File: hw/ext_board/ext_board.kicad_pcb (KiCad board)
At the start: 2 copper layers, 61 x 53.3 mm, 55 parts, among them Q1 SS8050, Q2 SS8050, Q3 SS8050, Q4 SS8050, Q5 SS8050, Q6 SS8050, Q7 SS8050, Q8 SS8050, Q9 SS8050, U1 74HC595PW, U2 74HC595PW, U3 M24LC16, U4 M93C76, X1 UNO_R3_CONN

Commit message: Add layout
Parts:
- added J1: Conn_01x03, Pin_Headers:Pin_Header_Straight_1x03_Pitch2.54mm, F.Cu at (127.0, 97.8)
- added J2: Conn_01x05, Pin_Headers:Pin_Header_Straight_1x05_Pitch2.54mm, F.Cu at (132.6, 97.8)
- added J3: Conn_01x03, Pin_Headers:Pin_Header_Straight_1x03_Pitch2.54mm, F.Cu at (180.3, 63.5)
- added J4: Conn_01x02, Pin_Headers:Pin_Header_Straight_1x02_Pitch2.54mm, F.Cu at (127.0, 111.2)
- added LD2: RGBW, ext_board:GNL-5050WRGB, F.Cu at (171.3, 91.4)
- C1, C2, C3, C4, C5, C6, D1, Q5, Q6, Q7, Q8, Q9, R1, R10, R11, R12, R13, R14, R15, R16, R17, R18, R19, R2, R20, R21, R22, R23, R24, R25, R26, R27, R7, R8, R9, U1, U2, U3, U4: moved to B.Cu
- moved C3 98.0 mm to (127.3, 70.1), turned to 180 degrees
- moved C1 92.0 mm to (155.8, 67.8), turned to 180 degrees
- moved R16 89.5 mm to (127.8, 68.1), turned to 180 degrees
- moved C2 89.4 mm to (164.0, 67.8), turned to 180 degrees
- moved C4 82.5 mm to (130.9, 80.6)
- moved R15 82.5 mm to (127.8, 66.3), turned to 180 degrees
- moved C6 78.8 mm to (169.0, 79.4), turned to 270 degrees
- moved R9 73.0 mm to (144.8, 85.7), turned to 270 degrees
- moved R19 69.0 mm to (178.6, 88.9), turned to 90 degrees
- moved R8 68.1 mm to (149.9, 77.1), turned to 270 degrees
- moved R12 67.0 mm to (141.9, 77.1), turned to 270 degrees
- moved R10 65.5 mm to (139.7, 85.7), turned to 270 degrees
- moved Q8 65.0 mm to (175.2, 95.5), turned to 180 degrees
- moved R13 62.0 mm to (147.3, 85.7), turned to 270 degrees
- moved R26 56.6 mm to (174.2, 82.8), turned to 90 degrees
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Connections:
- B1 pad 4: Net-(B1-Pad4) -> /QH2
- B2 pad 4: Net-(B2-Pad4) -> /QG2
- B3 pad 4: Net-(B3-Pad4) -> /QF2
- B4 pad 4: Net-(B4-Pad4) -> /QE2
- Q5 pad 3: (no net) -> Net-(LD2-Pad1)
- Q6 pad 3: (no net) -> Net-(LD2-Pad2)
- Q8 pad 3: (no net) -> Net-(LD2-Pad3)
- Q9 pad 3: (no net) -> Net-(LD2-Pad4)
- R10 pad 2: Net-(R10-Pad2) -> /QE1
- R11 pad 2: Net-(R11-Pad2) -> /QD1
- R12 pad 2: Net-(R12-Pad2) -> /QC1
- R13 pad 2: Net-(R13-Pad2) -> /QB1
- R14 pad 2: Net-(R14-Pad2) -> /QA1
- R23 pad 1: (no net) -> Net-(LD2-Pad8)
- R24 pad 1: (no net) -> Net-(LD2-Pad7)
- R26 pad 1: (no net) -> Net-(LD2-Pad6)
- R27 pad 1: (no net) -> Net-(LD2-Pad5)
- R3 pad 2: Net-(R3-Pad2) -> /QA2
- R4 pad 2: Net-(R4-Pad2) -> /QB2
- R5 pad 2: Net-(R5-Pad2) -> /QC2
- R6 pad 2: Net-(R6-Pad2) -> /QD2
- R7 pad 2: Net-(R7-Pad2) -> /QH1
- R8 pad 2: Net-(R8-Pad2) -> /QG1
- R9 pad 2: Net-(R9-Pad2) -> /QF1
- U1 pad 1: Net-(R13-Pad2) -> /QD2
- U1 pad 15: Net-(R14-Pad2) -> /QH2
- U1 pad 2: Net-(R12-Pad2) -> /QA2
- U1 pad 3: Net-(R11-Pad2) -> /QH1
- U1 pad 4: Net-(R10-Pad2) -> /QC1
- U1 pad 5: Net-(R9-Pad2) -> /QB2
- U1 pad 6: Net-(R8-Pad2) -> /QC2
- U1 pad 7: Net-(R7-Pad2) -> /QG1
- U2 pad 1: Net-(R4-Pad2) -> /QF2
- U2 pad 15: Net-(R3-Pad2) -> /QG2
- U2 pad 2: Net-(R5-Pad2) -> /QE2
- U2 pad 3: Net-(R6-Pad2) -> /QD1
- U2 pad 4: Net-(B4-Pad4) -> /QE1
- U2 pad 5: Net-(B3-Pad4) -> /QA1
- U2 pad 6: Net-(B2-Pad4) -> /QF1
- U2 pad 7: Net-(B1-Pad4) -> /QB1
- X1 pad 15: (no net) -> /RX
- X1 pad 16: (no net) -> /TX
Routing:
- net GND: track 0.00 -> 207.3 mm, vias 0 -> 14
- net +5V: track 0.00 -> 196.4 mm, vias 0 -> 8
- net /KEY: track 0.00 -> 96.6 mm, vias 0 -> 2
- net /SCK: track 0.00 -> 82.0 mm, vias 0 -> 1
- net /MOSI: track 0.00 -> 69.4 mm, vias 0 -> 2
- net /QH2: track 0.00 -> 55.9 mm, vias 0 -> 3
- net /~CS: track 0.00 -> 47.9 mm, vias 0 -> 1
- net /SDA: track 0.00 -> 45.9 mm, vias 0 -> 1
- net /MISO: track 0.00 -> 43.8 mm, vias 0 -> 1
- net /QD1: track 0.00 -> 38.8 mm
- net /CLK: track 0.00 -> 38.0 mm, vias 0 -> 1
- net Net-(R22-Pad1): track 0.00 -> 38.0 mm
- net /LEDW: track 0.00 -> 38.0 mm, vias 0 -> 1
- net /QE2: track 0.00 -> 37.4 mm, vias 0 -> 1
- net /QG2: track 0.00 -> 35.6 mm, vias 0 -> 1
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- added copper zone on B.Cu, net GND
- added copper zone on F.Cu, net GND
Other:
- net class Default: trace_width 0.25 -> 0.35; via_dia 0.6 -> 1; via_drill 0.4 -> 0.5
- rule via_min_size: 0.4 -> 0.9

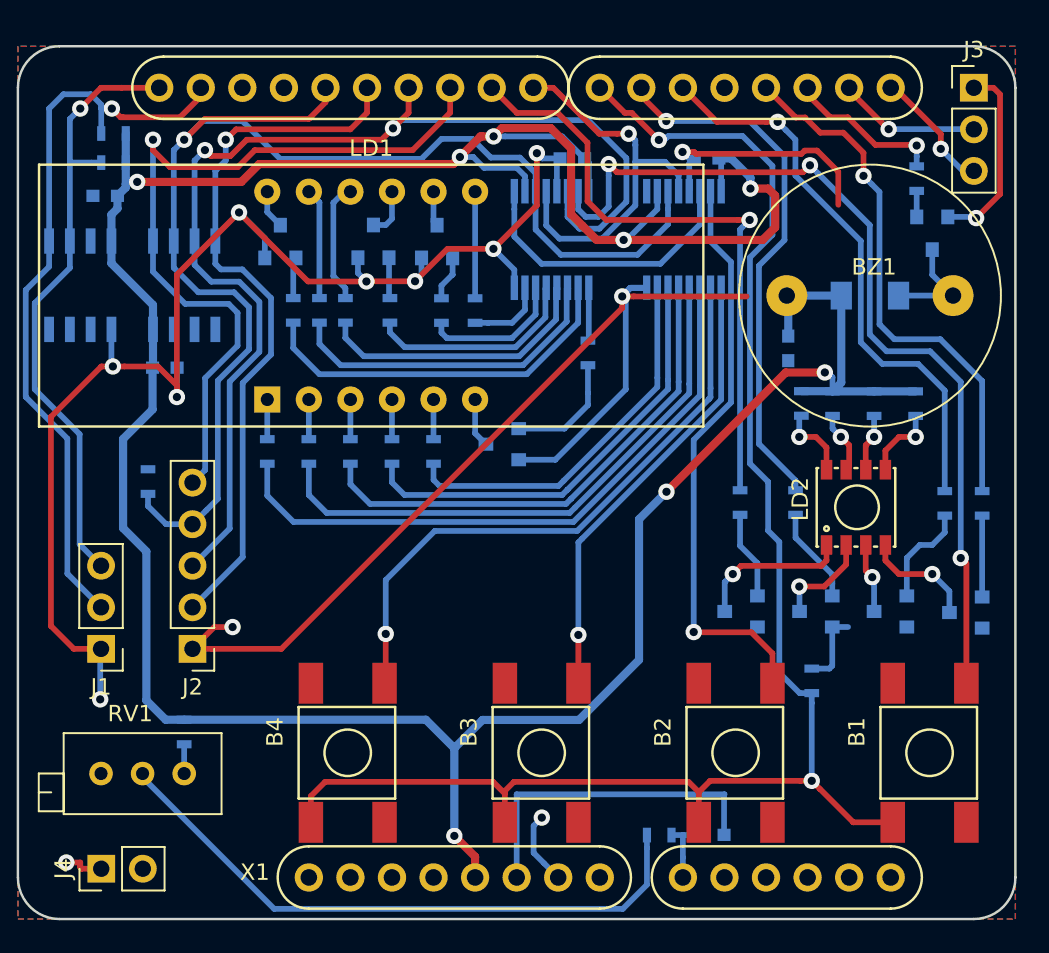
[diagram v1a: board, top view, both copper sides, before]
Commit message: Change buttons to TH
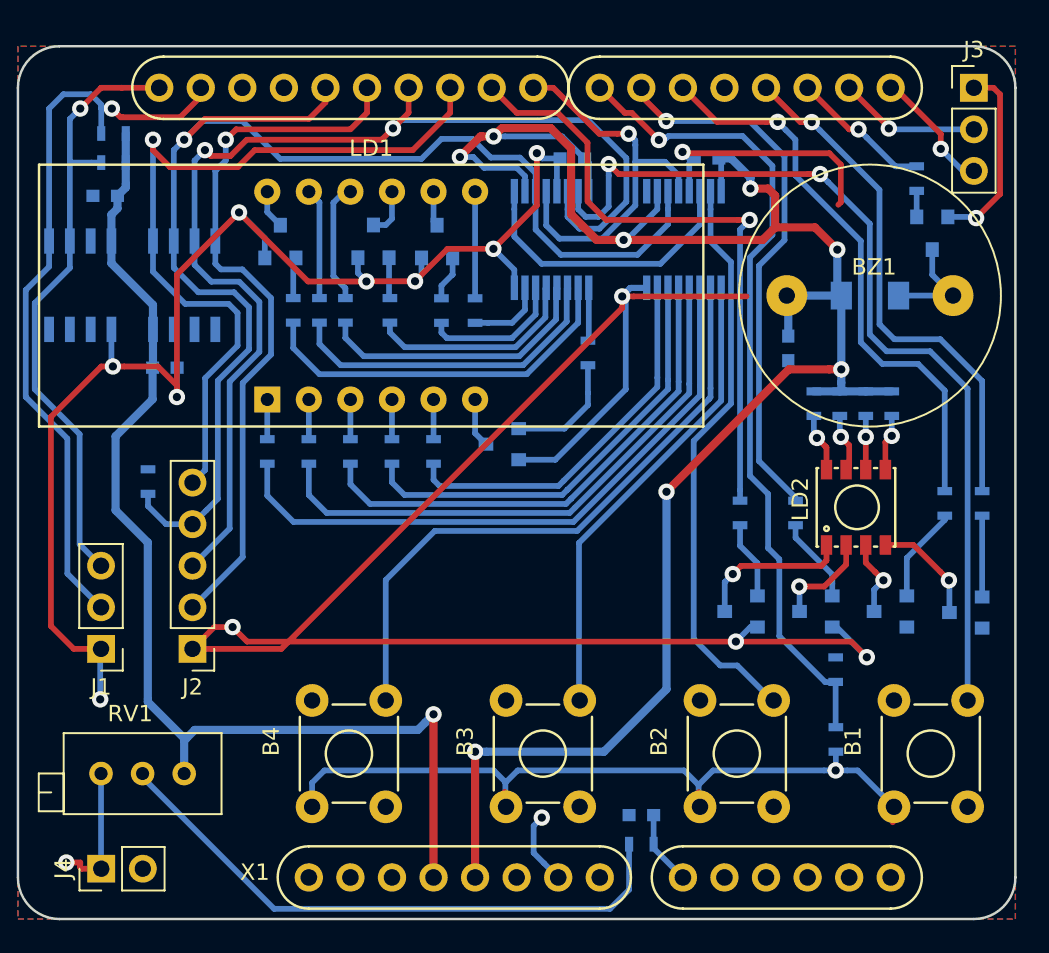
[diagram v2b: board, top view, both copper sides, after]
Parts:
- B1, B2, B3, B4: footprint ext_board:IT-1102WB_6x6x7 -> ext_board:KLS7-TS6601_6x6x4.3
- R25: value 6.7k -> 6.8k
- moved R25 39.8 mm to (171.9, 103.3), turned to 270 degrees
- moved C5 4.47 mm to (160.0, 108.0), turned to 180 degrees
- moved B3 3.95 mm to (151.8, 107.4)
- moved B4 3.95 mm to (139.9, 107.4)
- moved B1 3.95 mm to (175.5, 107.4)
- moved B2 3.95 mm to (163.6, 107.4)
- moved R2 1.61 mm to (171.9, 99.1)
- moved R27 1.46 mm to (175.3, 82.8)
- moved R22 1.23 mm to (160.0, 109.7)
- moved R23 0.76 mm to (170.6, 82.8)
- moved R17 0.64 mm to (166.1, 89.5)
- moved R18 0.64 mm to (169.4, 89.5)
- moved R26 0.51 mm to (173.7, 82.8)
- moved R24 0.44 mm to (172.1, 82.8)
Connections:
- net /QA1 renamed /LED_DP
- net /QA2 renamed /LED_1
- net /QB1 renamed /LED_G
- net /QB2 renamed /LED_2
- net /QC1 renamed /LED_F
- net /QC2 renamed /LED_3
- net /QD1 renamed /LED_E
- net /QD2 renamed /LED_4
- net /QE1 renamed /LED_D
- net /QE2 renamed /KEY_B4
- net /QF1 renamed /LED_C
- net /QF2 renamed /KEY_B3
- net /QG1 renamed /LED_B
- net /QG2 renamed /KEY_B2
- net /QH1 renamed /LED_A
- net /QH2 renamed /KEY_B1
- B1 pad 1: /KEY -> Net-(B1-Pad1)
- B2 pad 1: /KEY -> Net-(B1-Pad1)
- B3 pad 1: /KEY -> Net-(B1-Pad1)
- B4 pad 1: /KEY -> Net-(B1-Pad1)
- C3 pad 1: +5V -> +3V3
- C4 pad 1: +5V -> +3V3
- R15 pad 1: +5V -> +3V3
- R16 pad 1: +5V -> +3V3
- R25 pad 1: Net-(R25-Pad1) -> /KEY
- R25 pad 2: +5V -> Net-(B1-Pad1)
- RV1 pad 1: Net-(R25-Pad1) -> +3V3
- U3 pad 8: +5V -> +3V3
- U4 pad 8: +5V -> +3V3
- X1 pad 4: (no net) -> +3V3
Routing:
- net +5V: track 196.4 -> 122.4 mm
- net +3V3: track 0.00 -> 69.1 mm, vias 0 -> 1
- net /KEY: track 96.6 -> 50.5 mm, vias 2 -> 1
- net Net-(B1-Pad1): track 0.00 -> 45.4 mm, vias 0 -> 1
- net GND: track 207.3 -> 232.6 mm, vias 14 -> 16
- net Net-(R25-Pad1): track 1.79 -> 0.00 mm
- net Net-(R22-Pad1): track 38.0 -> 36.6 mm
- net Net-(LD2-Pad5): track 4.65 -> 3.45 mm
- net /KEY_B4: track 37.4 -> 38.5 mm, vias 1 -> 0
- net /KEY_B3: track 27.8 -> 28.8 mm, vias 1 -> 0
- net Net-(LD2-Pad8): track 4.64 -> 3.61 mm
- net /PWM: track 9.64 -> 8.66 mm
- net /KEY_B1: track 55.9 -> 56.7 mm, vias 3 -> 2
- net /LEDR: track 32.9 -> 32.2 mm
- net /LEDB: track 33.3 -> 33.9 mm
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
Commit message: Add reference signes
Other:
- board size 61 x 53.3 mm -> 63.5 x 55.9 mm
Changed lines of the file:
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@@
     (links 139)
     (no_connects 0)
-    (area 121.844999 60.884999 182.955001 114.375001)
+    (area 110.484367 54.45 189.095953 115.974219)
     (thickness 1.6)
-    (drawings 10)
+    (drawings 22)
     (tracks 683)
     (zones 0)
@@
     (34 B.Paste user)
     (35 F.Paste user)
-    (36 B.SilkS user hide)
+    (36 B.SilkS user)
     (37 F.SilkS user)
     (38 B.Mask user)
@@
     (46 B.CrtYd user)
     (47 F.CrtYd user)
-    (48 B.Fab user hide)
-    (49 F.Fab user hide)
+    (48 B.Fab user)
+    (49 F.Fab user)
   )
   (setup
@@
     (trace_min 0.2)
     (segment_width 0.2)
-    (edge_width 0.15)
+    (edge_width 0.1)
     (via_size 1)
     (via_drill 0.5)
@@
     (pad_to_mask_clearance 0.2)
     (aux_axis_origin 121.92 114.3)
-    (visible_elements FFFFFF7F)
+    (visible_elements FFFFFFFF)
     (pcbplotparams
       (layerselection 0x00030_80000001)
@@
     (pad 3 thru_hole circle (at 0 4.5 90) (size 2 2) (drill 1) (layers *.Cu *.Mask))
   )
+  (gr_line (start 120.65 60.96) (end 123.19 60.96) (layer Edge.Cuts) (width 0.1))
+  (gr_line (start 121.92 59.69) (end 121.92 62.23) (layer Edge.Cuts) (width 0.1))
+  (gr_circle (center 121.92 60.96) (end 122.555 60.96) (layer Edge.Cuts) (width 0.1))
+  (gr_line (start 181.61 60.96) (end 184.15 60.96) (layer Edge.Cuts) (width 0.1))
+  (gr_line (start 182.88 59.69) (end 182.88 62.23) (layer Edge.Cuts) (width 0.1))
+  (gr_circle (center 182.88 60.96) (end 183.515 60.96) (layer Edge.Cuts) (width 0.1))
+  (gr_line (start 181.61 114.3) (end 184.15 114.3) (layer Edge.Cuts) (width 0.1))
+  (gr_line (start 182.88 113.03) (end 182.88 115.57) (layer Edge.Cuts) (width 0.1))
+  (gr_circle (center 182.88 114.3) (end 183.515 114.3) (layer Edge.Cuts) (width 0.1))
+  (gr_line (start 121.92 113.03) (end 121.92 115.57) (layer Edge.Cuts) (width 0.1))
+  (gr_line (start 120.65 114.3) (end 123.19 114.3) (layer Edge.Cuts) (width 0.1))
+  (gr_circle (center 121.92 114.3) (end 122.555 114.3) (layer Edge.Cuts) (width 0.1))
   (dimension 53.34 (width 0.3) (layer Dwgs.User)
     (gr_text "53.340 mm" (at 116.984366 87.63 90) (layer Dwgs.User)

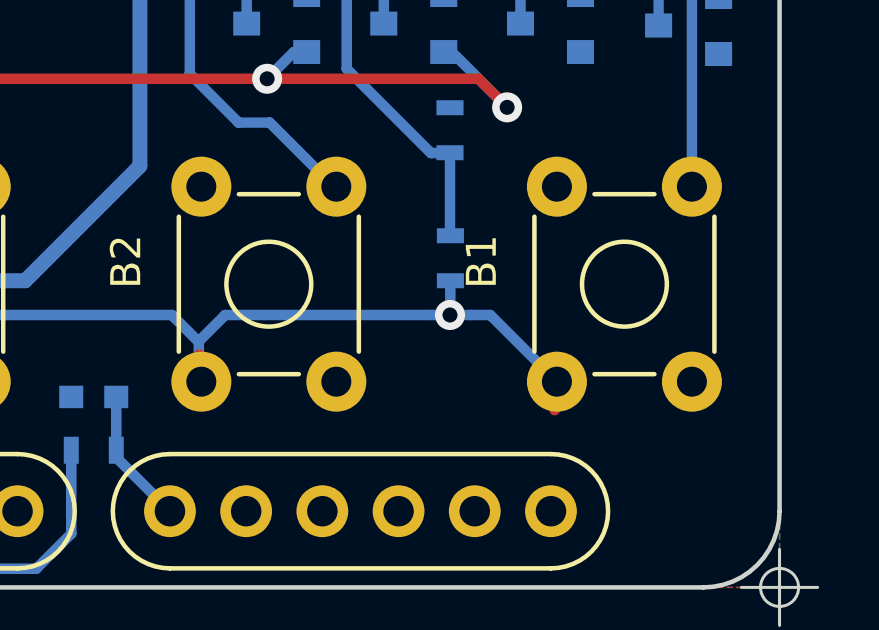
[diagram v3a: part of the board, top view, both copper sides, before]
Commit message: Remove useless via
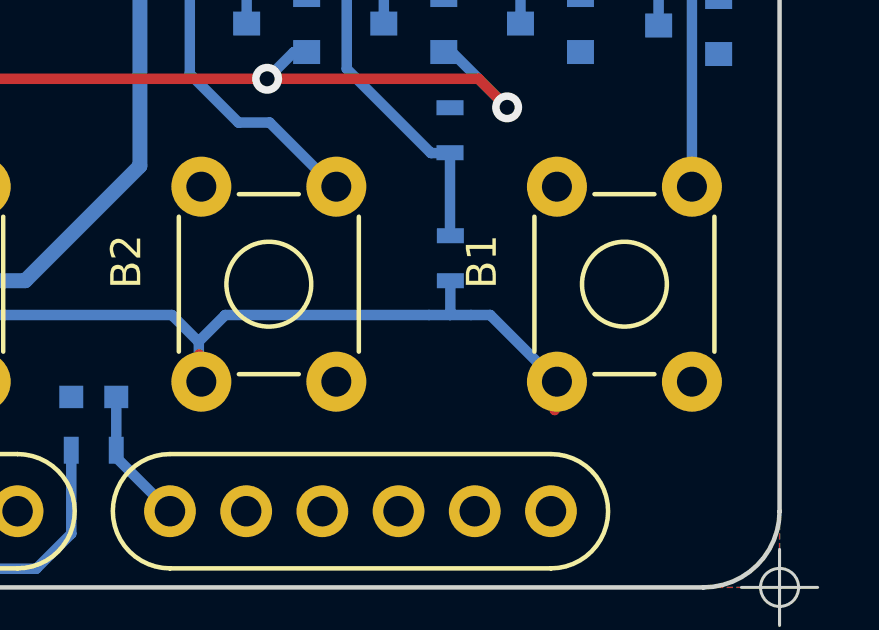
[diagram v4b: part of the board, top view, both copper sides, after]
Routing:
- net Net-(B1-Pad1): vias 1 -> 0
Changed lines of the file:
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@@
     (thickness 1.6)
     (drawings 22)
-    (tracks 683)
+    (tracks 682)
     (zones 0)
     (modules 60)
@@
     (visible_elements FFFFFFFF)
     (pcbplotparams
-      (layerselection 0x00030_80000001)
+      (layerselection 0x00000_80000001)
       (usegerberextensions false)
-      (excludeedgelayer true)
+      (excludeedgelayer false)
       (linewidth 0.100000)
       (plotframeref false)
@@
       (padsonsilk false)
       (subtractmaskfromsilk false)
-      (outputformat 1)
+      (outputformat 3)
       (mirror false)
-      (drillshape 1)
+      (drillshape 2)
       (scaleselection 1)
-      (outputdirectory ""))
+      (outputdirectory cam/))
   )
   (net 0 "")
@@
   (segment (start 172.601606 105.2195) (end 171.8945 105.2195) (width 0.35) (layer B.Cu) (net 51))
   (segment (start 175.459 107.442) (end 173.2365 105.2195) (width 0.35) (layer B.Cu) (net 51))
-  (via (at 171.8945 105.2195) (size 1) (drill 0.5) (layers F.Cu B.Cu) (net 51))
   (segment (start 151.71 105.973) (end 151.71 105.9265) (width 0.35) (layer B.Cu) (net 51))
   (segment (start 151.71 105.9265) (end 151.003 105.2195) (width 0.35) (layer B.Cu) (net 51))
